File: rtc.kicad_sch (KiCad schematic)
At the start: 16 parts, among them U36 74LS05, U9 MSM6242B, Y9 32768

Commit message: DRAM chips replaced with SIMM module
Added logic to decode 2MB chip + 1.5MB slow
Rewired trapdoor slot
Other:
- title: Rämixx500 -> Rämixx500_max
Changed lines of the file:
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@@
 	(paper "A4")
 	(title_block
-		(title "Rämixx500")
-		(date "2021-05-23")
-		(rev "1")
+		(title "Rämixx500_max")
+		(date "2026-03-13")
+		(rev "2")
 		(company "SukkoPera")
 		(comment 4 "Licensed under CC BY-NC-SA 4.0")

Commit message: Completed routing, no DRC errors (but still a lot of warnings)
TODO: thoroughly review all small schematic changes
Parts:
- JP9: now left out of the parts list
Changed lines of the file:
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@@
 	(title_block
 		(title "Rämixx500_max")
-		(date "2026-03-13")
-		(rev "2")
+		(date "2026-03-25")
+		(rev "3")
 		(company "SukkoPera")
 		(comment 4 "Licensed under CC BY-NC-SA 4.0")
@@
 		(unit 1)
 		(exclude_from_sim no)
-		(in_bom yes)
+		(in_bom no)
 		(on_board yes)
 		(dnp no)

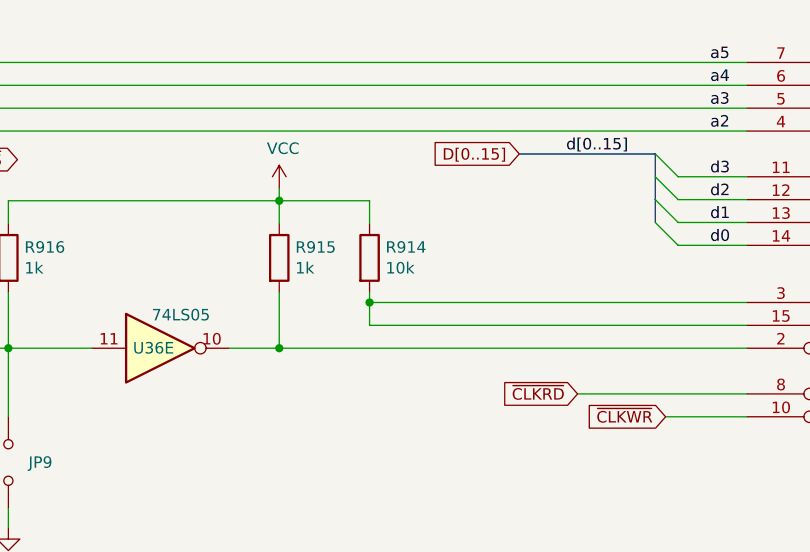
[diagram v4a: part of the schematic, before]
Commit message: Started cleaning up BOM
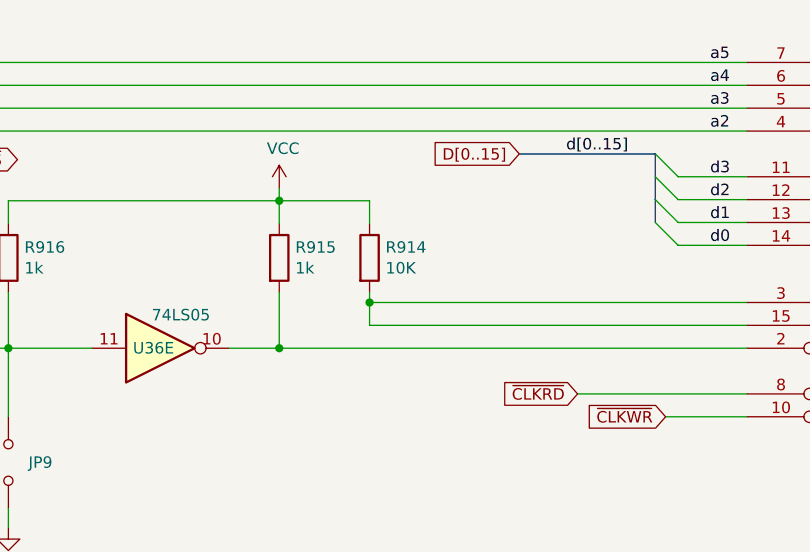
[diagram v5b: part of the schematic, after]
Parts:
- R914: value 10k -> 10K
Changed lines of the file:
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@@
 			)
 		)
-		(property "Value" "10k"
+		(property "Value" "10K"
 			(at 143.891 55.245 0)
 			(effects

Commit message: Working on BOM
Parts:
- BT9: MFG Name (none) -> Eagle Plastic Devices; MFG Part Num (none) -> 122-2420-GR; Mouser (none) -> 122-2420-GR
- C9: MFG Part Num C412C334M5U5TA -> C440C334K5R5TA7200; Mouser (none) -> 80-C440C334K5R-TR
- C911: MFG Name AVX -> KEMET; MFG Part Num SA102A220JARC -> C410C220J1G5TA; Mouser (none) -> 80-C410C220J1G
- C913: MFG Name RS PRO -> PANASONIC; MFG Part Num 181-4685 -> ECA-2AM4R7B; Mouser (none) -> 667-ECA-2AM4R7B
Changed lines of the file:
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@@
+			)
+		)
+		(property "Mouser" ""
+			(at 203.073 53.975 0)
+			(effects
+				(font
+					(size 1.27 1.27)
+				)
+				(hide yes)
 			)
 		)
@@
 			)
 		)
+		(property "Mouser" ""
+			(at 118.872 64.135 0)
+			(effects
+				(font
+					(size 1.27 1.27)
+				)
+				(hide yes)
+			)
+		)
 		(pin "2"
 		)
@@
 			)
 		)
+		(property "Mouser" ""
+			(at 132.08 54.102 0)
+			(effects
+				(font
+					(size 1.27 1.27)
+				)
+				(hide yes)
+			)
+		)
 		(pin "1"
 		)
@@
 			)
 		)
+		(property "Mouser" ""
+			(at 142.113 54.102 0)
+			(effects
+				(font
+					(size 1.27 1.27)
+				)
+				(hide yes)
+			)
+		)
 		(pin "1"
 		)
@@
 			)
 		)
+		(property "Mouser" ""
+			(at 101.981 54.102 0)
+			(effects
+				(font
+					(size 1.27 1.27)
+				)
+				(hide yes)
+			)
+		)
 		(pin "2"
 		)
@@
 			)
 		)
+		(property "Mouser" ""
+			(at 101.981 76.835 90)
+			(effects
+				(font
+					(size 1.27 1.27)
+				)
+				(hide yes)
+			)
+		)
 		(pin "1"
 		)
@@
 			)
 		)
+		(property "Mouser" ""
+			(at 244.856 59.055 90)
+			(effects
+				(font
+					(size 1.27 1.27)
+				)
+				(hide yes)
+			)
+		)
 		(pin "1"
 		)
@@
 			)
 		)
-		(property "MFG Name" "AVX"
+		(property "MFG Name" "KEMET"
 			(at 244.856 69.215 0)
 			(effects
@@
 			)
 		)
-		(property "MFG Part Num" "SA102A220JARC"
+		(property "MFG Part Num" "C410C220J1G5TA "
 			(at 244.856 69.215 0)
+			(effects
+				(font
+					(size 1.27 1.27)
+				)
+				(hide yes)
+			)
+		)
+		(property "Mouser" "80-C410C220J1G "
+			(at 244.856 69.215 90)
 			(effects
 				(font
@@
 			)
 		)
+		(property "Mouser" ""
+			(at 80.518 64.135 0)
+			(effects
+				(font
+					(size 1.27 1.27)
+				)
+				(hide yes)
+			)
+		)
 		(pin "13"
 		)
@@
 			)
 		)
+		(property "Mouser" ""
+			(at 233.045 64.135 90)
+			(effects
+				(font
+					(size 1.27 1.27)
+				)
+				(hide yes)
+			)
+		)
 		(pin "3"
 		)
@@
 			)
 		)
+		(property "MFG Name" "Eagle Plastic Devices"
+			(at 74.93 149.098 0)
+			(effects
+				(font
+					(size 1.27 1.27)
+				)
+				(hide yes)
+			)
+		)
+		(property "MFG Part Num" "122-2420-GR"
+			(at 74.93 149.098 0)
+			(effects
+				(font
+					(size 1.27 1.27)
+				)
+				(hide yes)
+			)
+		)
+		(property "Mouser" "122-2420-GR"
+			(at 74.93 149.098 0)
+			(effects
+				(font
+					(size 1.27 1.27)
+				)
+				(hide yes)
+			)
+		)
 		(pin "1"
 		)
@@
 			)
 		)
-		(property "MFG Name" "RS PRO"
+		(property "MFG Name" "PANASONIC"
 			(at 96.647 147.828 0)
 			(effects
@@
 			)
 		)
-		(property "MFG Part Num" "181-4685"
+		(property "MFG Part Num" "ECA-2AM4R7B "
+			(at 96.647 147.828 0)
+			(effects
+				(font
+					(size 1.27 1.27)
+				)
+				(hide yes)
+			)
+		)
+		(property "Mouser" "667-ECA-2AM4R7B"
 			(at 96.647 147.828 0)
 			(effects
@@
 			)
 		)
+		(property "Mouser" ""
+			(at 115.697 147.955 0)
+			(effects
+				(font
+					(size 1.27 1.27)
+				)
+				(hide yes)
+			)
+		)
 		(pin "5"
 		)
@@
 			)
 		)
-		(property "MFG Part Num" "C412C334M5U5TA"
+		(property "MFG Part Num" "C440C334K5R5TA7200"
 			(at 139.446 147.828 0)
 			(effects
@@
 		)
 		(property "Section" "RTC"
+			(at 139.446 147.828 0)
+			(effects
+				(font
+					(size 1.27 1.27)
+				)
+				(hide yes)
+			)
+		)
+		(property "Mouser" "80-C440C334K5R-TR "
 			(at 139.446 147.828 0)
 			(effects
@@
 			)
 		)
+		(property "Mouser" ""
+			(at 96.647 119.888 90)
+			(effects
+				(font
+					(size 1.27 1.27)
+				)
+				(hide yes)
+			)
+		)
 		(pin "1"
 		)
@@
 			)
 		)
+		(property "Mouser" ""
+			(at 104.013 112.522 0)
+			(effects
+				(font
+					(size 1.27 1.27)
+				)
+				(hide yes)
+			)
+		)
 		(pin "2"
 		)
@@
 			)
 		)
+		(property "Mouser" ""
+			(at 88.519 112.522 90)
+			(effects
+				(font
+					(size 1.27 1.27)
+				)
+				(hide yes)
+			)
+		)
 		(pin "1"
 		)
@@
 			(at 85.471 129.54 0)
 			(effects
+				(font
+					(size 1.27 1.27)
+				)
+				(hide yes)
+			)
+		)
+		(property "Mouser" ""
+			(at 85.471 129.54 0)
+			(effects

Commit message: more work on BOM done
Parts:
- D911, D912, D913: value 1n4148 -> 1N4148; MFG Name (none) -> ONSEMI; MFG Part Num (none) -> 1N4148TR; Mouser (none) -> 512-1N4148TR
- R911: MFG Name (none) -> YAGEO; MFG Part Num (none) -> MFR-25FBF52-470R; Mouser (none) -> 603-MFR-25FBF52-470R
- R914: MFG Name (none) -> YAGEO; MFG Part Num (none) -> MFR-25FBF52-10K; Mouser (none) -> 603-MFR-25FBF52-10K
- R915, R916: MFG Name (none) -> YAGEO; MFG Part Num (none) -> MFR-25FBF52-1K; Mouser (none) -> 603-MFR-25FBF52-1K
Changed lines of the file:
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@@
 			)
 		)
-		(property "Mouser" ""
+		(property "Mouser" "603-MFR-25FBF52-1K "
+			(at 132.08 54.102 0)
+			(effects
+				(font
+					(size 1.27 1.27)
+				)
+				(hide yes)
+			)
+		)
+		(property "MFG Name" "YAGEO"
+			(at 132.08 54.102 0)
+			(effects
+				(font
+					(size 1.27 1.27)
+				)
+				(hide yes)
+			)
+		)
+		(property "MFG Part Num" "MFR-25FBF52-1K"
 			(at 132.08 54.102 0)
 			(effects
@@
 			)
 		)
-		(property "Mouser" ""
+		(property "Mouser" "603-MFR-25FBF52-10K"
+			(at 142.113 54.102 0)
+			(effects
+				(font
+					(size 1.27 1.27)
+				)
+				(hide yes)
+			)
+		)
+		(property "MFG Name" "YAGEO"
+			(at 142.113 54.102 0)
+			(effects
+				(font
+					(size 1.27 1.27)
+				)
+				(hide yes)
+			)
+		)
+		(property "MFG Part Num" "MFR-25FBF52-10K"
 			(at 142.113 54.102 0)
 			(effects
@@
 			)
 		)
-		(property "Mouser" ""
+		(property "Mouser" "603-MFR-25FBF52-1K "
+			(at 101.981 54.102 0)
+			(effects
+				(font
+					(size 1.27 1.27)
+				)
+				(hide yes)
+			)
+		)
+		(property "MFG Name" "YAGEO"
+			(at 101.981 54.102 0)
+			(effects
+				(font
+					(size 1.27 1.27)
+				)
+				(hide yes)
+			)
+		)
+		(property "MFG Part Num" "MFR-25FBF52-1K"
 			(at 101.981 54.102 0)
 			(effects
@@
 			)
 		)
-		(property "Value" "1n4148"
+		(property "Value" "1N4148"
 			(at 98.6536 121.031 90)
 			(effects
@@
 			)
 		)
-		(property "Mouser" ""
+		(property "Mouser" "512-1N4148TR "
+			(at 96.647 119.888 90)
+			(effects
+				(font
+					(size 1.27 1.27)
+				)
+				(hide yes)
+			)
+		)
+		(property "MFG Name" "ONSEMI"
+			(at 96.647 119.888 90)
+			(effects
+				(font
+					(size 1.27 1.27)
+				)
+				(hide yes)
+			)
+		)
+		(property "MFG Part Num" "1N4148TR"
 			(at 96.647 119.888 90)
 			(effects
@@
 			)
 		)
-		(property "Value" "1n4148"
+		(property "Value" "1N4148"
 			(at 104.013 109.347 0)
 			(effects
@@
 			)
 		)
-		(property "Mouser" ""
+		(property "Mouser" "512-1N4148TR "
+			(at 104.013 112.522 0)
+			(effects
+				(font
+					(size 1.27 1.27)
+				)
+				(hide yes)
+			)
+		)
+		(property "MFG Name" "ONSEMI"
+			(at 104.013 112.522 0)
+			(effects
+				(font
+					(size 1.27 1.27)
+				)
+				(hide yes)
+			)
+		)
+		(property "MFG Part Num" "1N4148TR"
 			(at 104.013 112.522 0)
 			(effects
@@
 			)
 		)
-		(property "Mouser" ""
+		(property "Mouser" "603-MFR-25FBF52-470R"
+			(at 88.519 112.522 90)
+			(effects
+				(font
+					(size 1.27 1.27)
+				)
+				(hide yes)
+			)
+		)
+		(property "MFG Name" "YAGEO"
+			(at 88.519 112.522 90)
+			(effects
+				(font
+					(size 1.27 1.27)
+				)
+				(hide yes)
+			)
+		)
+		(property "MFG Part Num" "MFR-25FBF52-470R"
 			(at 88.519 112.522 90)
 			(effects
@@
 			)
 		)
-		(property "Value" "1n4148"
+		(property "Value" "1N4148"
 			(at 85.471 126.365 0)
 			(effects
@@
 			)
 		)
-		(property "Mouser" ""
+		(property "Mouser" "512-1N4148TR "
 			(at 85.471 129.54 0)
 			(effects
+				(font
+					(size 1.27 1.27)
+				)
+				(hide yes)
+			)
+		)
+		(property "MFG Name" "ONSEMI"
+			(at 85.471 129.54 0)
+			(effects
+				(font
+					(size 1.27 1.27)
+				)
+				(hide yes)
+			)
+		)
+		(property "MFG Part Num" "1N4148TR"
+			(at 85.471 129.54 0)
+			(effects

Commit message: BOM updates
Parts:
- TC9: value 6.8-45p -> 12pF - 40pF; MFG Name (none) -> JML06-1; MFG Part Num (none) -> JML06-1 / 40PF / YELLOW
- U36: MFG Part Num SN74LS05N -> SN74LS05N; Mouser (none) -> 595-SN74LS05N
- Y9: value 32768 -> 32.768kHz; MFG Name (none) -> ECS; MFG Part Num (none) -> ECS-.327-12.5-13X; Mouser (none) -> 520-TFC2X6-X
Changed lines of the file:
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@@
 			)
 		)
-		(property "MFG Part Num" "SN74LS05N"
+		(property "MFG Part Num" "SN74LS05N "
 			(at 118.872 64.135 0)
 			(effects
@@
 			)
 		)
-		(property "Mouser" ""
+		(property "Mouser" "595-SN74LS05N "
 			(at 118.872 64.135 0)
 			(effects
@@
 			)
 		)
-		(property "Value" "6.8-45p"
+		(property "Value" "12pF - 40pF"
 			(at 244.856 54.9656 90)
 			(effects
@@
 			)
 		)
-		(property "Datasheet" "~"
+		(property "Datasheet" "https://www.electrokit.com/upload/product/41016/41016014/JML06-4.pdf"
 			(at 244.856 59.055 0)
 			(effects
@@
 		)
 		(property "Mouser" ""
+			(at 244.856 59.055 90)
+			(effects
+				(font
+					(size 1.27 1.27)
+				)
+				(hide yes)
+			)
+		)
+		(property "MFG Part Num" "JML06-1 / 40PF / YELLOW"
+			(at 244.856 59.055 90)
+			(effects
+				(font
+					(size 1.27 1.27)
+				)
+				(hide yes)
+			)
+		)
+		(property "MFG Name" "JML06-1"
 			(at 244.856 59.055 90)
 			(effects
@@
 			)
 		)
-		(property "MFG Part Num" "SN74LS05N"
+		(property "MFG Part Num" "SN74LS05N "
 			(at 80.518 64.135 0)
 			(effects
@@
 			)
 		)
-		(property "Mouser" ""
+		(property "Mouser" "595-SN74LS05N "
 			(at 80.518 64.135 0)
 			(effects
@@
 			)
 		)
-		(property "Value" "32768"
+		(property "Value" "32.768kHz"
 			(at 229.997 71.374 90)
 			(effects
@@
 			)
 		)
-		(property "Mouser" ""
+		(property "Mouser" "520-TFC2X6-X "
 			(at 233.045 64.135 90)
 			(effects
+				(font
+					(size 1.27 1.27)
+				)
+				(hide yes)
+			)
+		)
+		(property "MFG Name" "ECS"
+			(at 233.045 64.135 90)
+			(effects
+				(font
+					(size 1.27 1.27)
+				)
+				(hide yes)
+			)
+		)
+		(property "MFG Part Num" "ECS-.327-12.5-13X "
+			(at 233.045 64.135 90)
+			(effects
